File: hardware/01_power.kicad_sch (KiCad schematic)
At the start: 0 parts

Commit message: Power sheet: USB input, rail split, analog LDO
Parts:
- added C1, C2: 1uF, symbol Device:C
- added J1: USB_5V_IN, Connector_RJ:RJ45_Abracon_ARJP11A-MA_Horizontal, symbol Connector_Generic:Conn_01x02
- added R1: 0R, Package_TO_SOT_THT:TO-92_Inline, symbol Device:R
- added U1: MCP1700-3302E/T0, Package_TO_SOT_THT:TO-92_Inline, symbol Regulator_Linear:MCP1700x-330xxTO
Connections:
- new net: C1.1, R1.2, U1.2 (VI)
- new net +3V3_A: C2.1, U1.3 (VO)
- new net +5V: J1.1 (Pin_1), R1.1
- new net GND: C1.2, C2.2, J1.2 (Pin_2), U1.1 (GND)
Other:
- note added: "C1, C2: 1uF per MCP1700 DS20001826F. C2 sets stability; C1 is input decoupling."

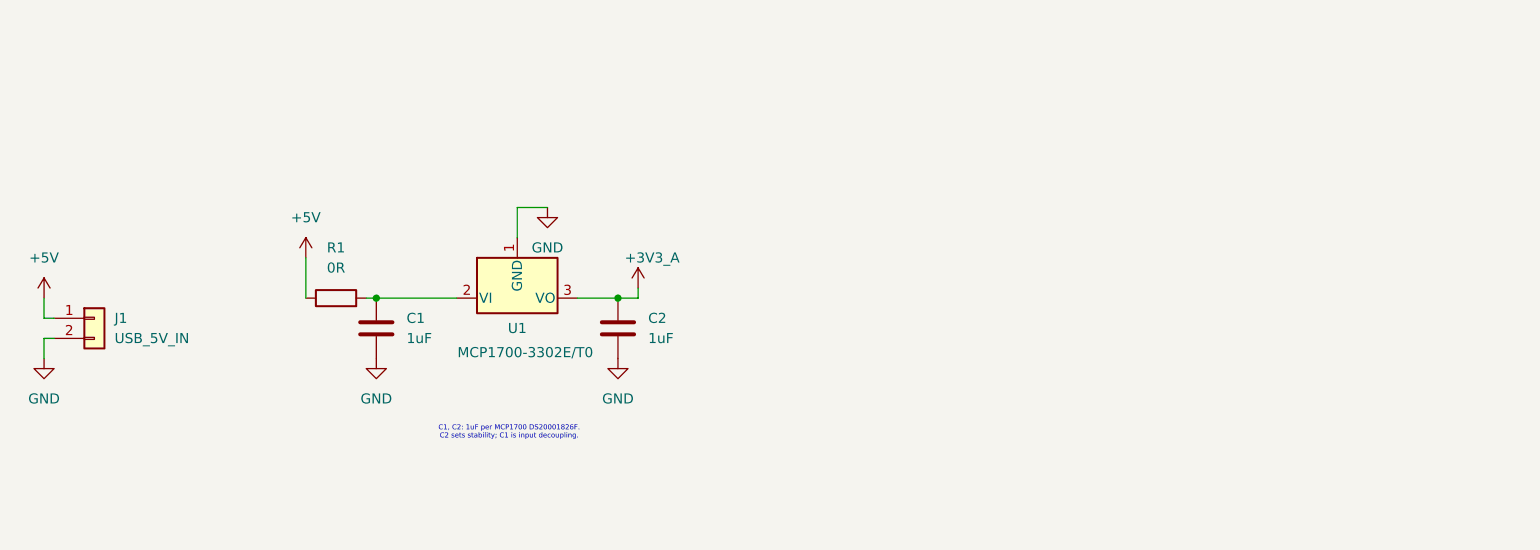
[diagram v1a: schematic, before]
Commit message: Power sheet: analog rail, rail split, 2.2 V reference
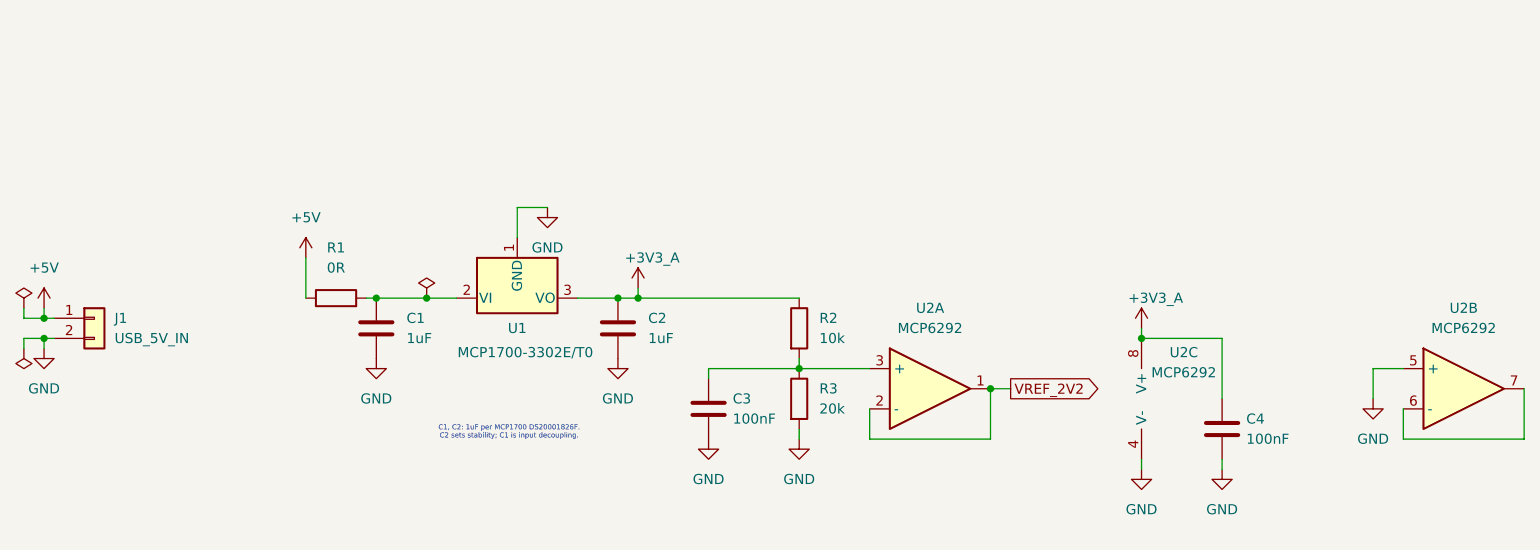
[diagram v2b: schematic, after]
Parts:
- added C3, C4: 100nF, symbol Device:C
- added R2: 10k, symbol Device:R
- added R3: 20k, symbol Device:R
- added U2: MCP6292, Package_TO_SOT_SMD:SOT-353_SC-70-5, symbol Amplifier_Operational:Opamp_Dual
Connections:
- net +3V3_A: now also C4.1, R2.1, U2.8 (V+)
- net GND: now also C3.2, C4.2, R3.2, U2.4 (V-), U2.5 (+)
- new net: U2.6 (-), U2.7
- new net: C3.1, R2.2, R3.1, U2.3 (+)
- new net VREF_2V2: U2.1, U2.2 (-)

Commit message: Add final Rev A schematic PDF and edited footprints
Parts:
- C1, C2, C3, C4: footprint (none) -> Capacitor_THT:C_Disc_D5.0mm_W2.5mm_P5.00mm
- J1: footprint Connector_RJ:RJ45_Abracon_ARJP11A-MA_Horizontal -> Connector_PinHeader_2.54mm:PinHeader_1x02_P2.54mm_Vertical
- R1: footprint Package_TO_SOT_THT:TO-92_Inline -> Resistor_THT:R_Axial_DIN0207_L6.3mm_D2.5mm_P10.16mm_Horizontal
- R2, R3: footprint (none) -> Resistor_THT:R_Axial_DIN0207_L6.3mm_D2.5mm_P10.16mm_Horizontal
- U2: footprint Package_TO_SOT_SMD:SOT-353_SC-70-5 -> Package_DIP:DIP-8_W7.62mm
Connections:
- net +5V_A: now reaches C1.1, R1.2, U1.2 (VI)
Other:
- company: (none) -> Paul Simbulan
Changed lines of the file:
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@@
 	(title_block
 		(title "Oscil")
-		(date "2026-09-18")
-		(rev "0.1")
+		(date "2026-09-21")
+		(rev "A")
+		(company "Paul Simbulan")
 		(comment 1 "Two-channel Digital Oscilloscope and Function Generator")
 		(comment 2 "ESP32-S3 / ESP-IDF / FreeRTOS")
+		(comment 3 "Rev A: breadboard build on ESP32-S3 dev boards")
 	)
 	(text ""
@@
 	)
 	(junction
+		(at 93.98 59.69)
+		(diameter 0)
+		(color 0 0 0 0)
+	)
+	(junction
 		(at 144.78 68.58)
 		(diameter 0)
@@
 	(wire
 		(pts
+			(xy 93.98 59.69) (xy 97.79 59.69)
+		)
+		(stroke
+			(width 0)
+			(type default)
+		)
+	)
+	(wire
+		(pts
 			(xy 144.78 68.58) (xy 153.67 68.58)
 		)
@@
 	(wire
 		(pts
-			(xy 91.44 59.69) (xy 97.79 59.69)
+			(xy 91.44 59.69) (xy 93.98 59.69)
 		)
 		(stroke
@@
 	(wire
 		(pts
+			(xy 93.98 53.34) (xy 93.98 59.69)
+		)
+		(stroke
+			(width 0)
+			(type default)
+		)
+	)
+	(wire
+		(pts
 			(xy 187.96 63.5) (xy 187.96 64.77)
 		)
@@
 			(width 0)
 			(type default)
+		)
+	)
+	(label "+5V_A"
+		(at 93.98 53.34 0)
+		(effects
+			(font
+				(size 1.27 1.27)
+			)
+			(justify left bottom)
 		)
 	)
@@
 			)
 		)
-		(property "Footprint" ""
+		(property "Footprint" "Capacitor_THT:C_Disc_D5.0mm_W2.5mm_P5.00mm"
 			(at 92.4052 67.31 0)
 			(hide yes)
@@
 			)
 		)
-		(property "Footprint" ""
+		(property "Footprint" "Capacitor_THT:C_Disc_D5.0mm_W2.5mm_P5.00mm"
 			(at 122.8852 67.31 0)
 			(hide yes)
@@
 			)
 		)
-		(property "Footprint" "Connector_RJ:RJ45_Abracon_ARJP11A-MA_Horizontal"
+		(property "Footprint" "Connector_PinHeader_2.54mm:PinHeader_1x02_P2.54mm_Vertical"
 			(at 55.88 62.23 0)
 			(hide yes)
@@
 			)
 		)
-		(property "Footprint" "Package_TO_SOT_SMD:SOT-353_SC-70-5"
+		(property "Footprint" "Package_DIP:DIP-8_W7.62mm"
 			(at 228.6 71.12 0)
 			(hide yes)
@@
 			)
 		)
-		(property "Footprint" ""
+		(property "Footprint" "Resistor_THT:R_Axial_DIN0207_L6.3mm_D2.5mm_P10.16mm_Horizontal"
 			(at 143.002 63.5 90)
 			(hide yes)
@@
 			)
 		)
-		(property "Footprint" "Package_TO_SOT_SMD:SOT-353_SC-70-5"
+		(property "Footprint" "Package_DIP:DIP-8_W7.62mm"
 			(at 161.29 71.12 0)
 			(hide yes)
@@
 			)
 		)
-		(property "Footprint" "Package_TO_SOT_THT:TO-92_Inline"
+		(property "Footprint" "Resistor_THT:R_Axial_DIN0207_L6.3mm_D2.5mm_P10.16mm_Horizontal"
 			(at 86.36 61.468 90)
 			(hide yes)
@@
 			)
 		)
-		(property "Footprint" ""
+		(property "Footprint" "Capacitor_THT:C_Disc_D5.0mm_W2.5mm_P5.00mm"
 			(at 199.0852 80.01 0)
 			(hide yes)
@@
 			)
 		)
-		(property "Footprint" ""
+		(property "Footprint" "Capacitor_THT:C_Disc_D5.0mm_W2.5mm_P5.00mm"
 			(at 134.3152 77.47 0)
 			(hide yes)
@@
 			)
 		)
-		(property "Footprint" ""
+		(property "Footprint" "Resistor_THT:R_Axial_DIN0207_L6.3mm_D2.5mm_P10.16mm_Horizontal"
 			(at 143.002 72.39 90)
 			(hide yes)
@@
 			)
 		)
-		(property "Footprint" "Package_TO_SOT_SMD:SOT-353_SC-70-5"
+		(property "Footprint" "Package_DIP:DIP-8_W7.62mm"
 			(at 190.5 72.39 0)
 			(hide yes)

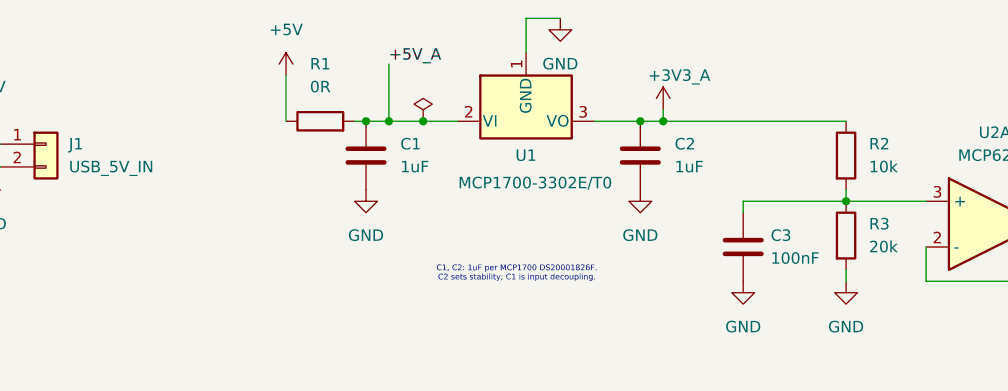
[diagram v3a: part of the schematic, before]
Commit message: hardware: bulk decoupling on the analog rail and ADC VDD, VREF filter, analog parts on +3V3_A
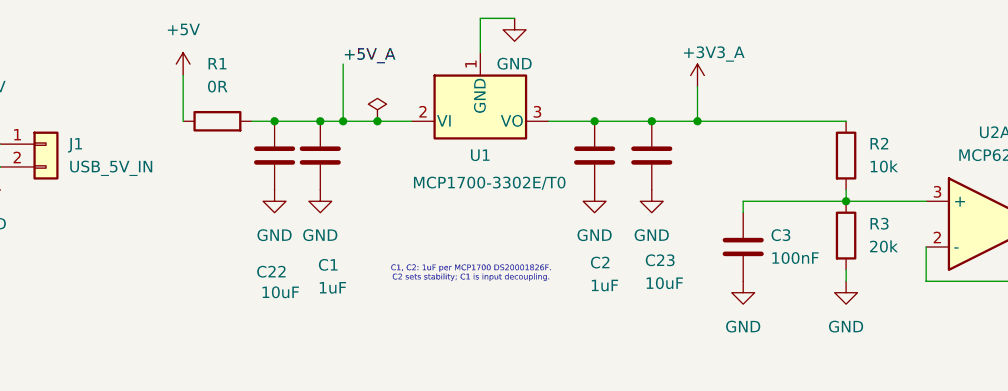
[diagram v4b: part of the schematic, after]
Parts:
- added C22, C23: 10uF, Capacitor_THT:C_Disc_D5.0mm_W2.5mm_P5.00mm, symbol Device:C
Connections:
- net +3V3_A: now also C23.1
- net +5V_A: now also C22.1
- net GND: now also C22.2, C23.2
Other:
- moved on the sheet: C1, C2, R1, U1

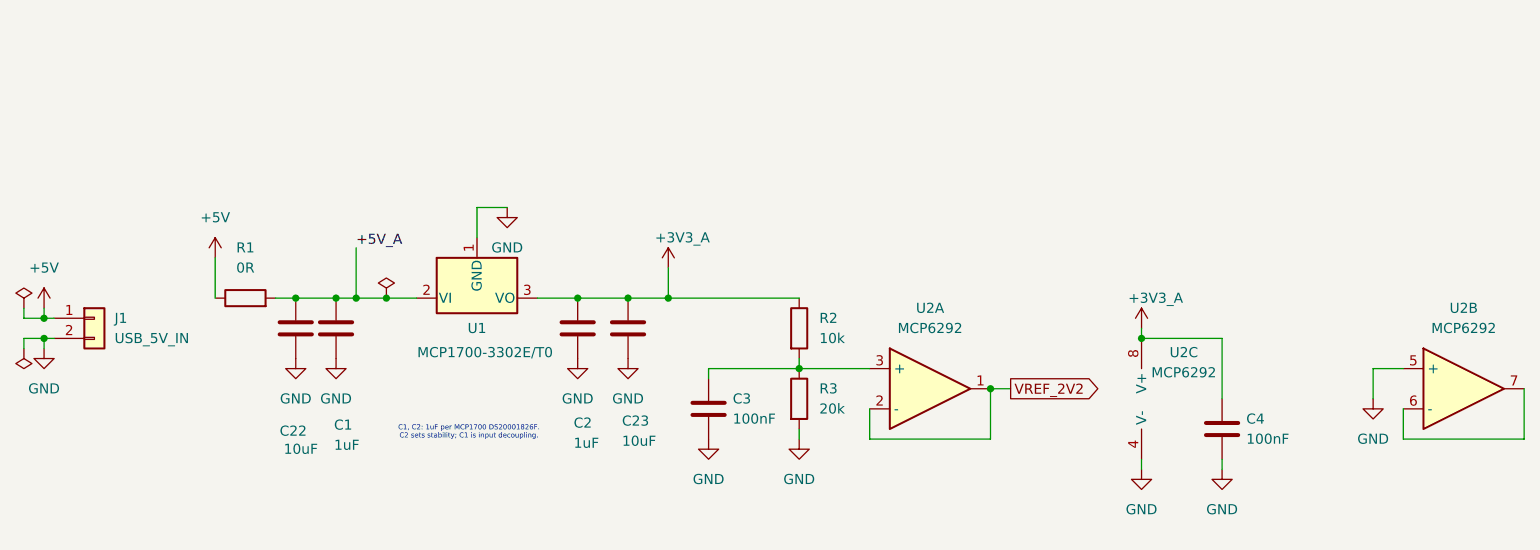
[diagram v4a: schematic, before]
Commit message: hardware: 220R series on each link line, analog decoupling notes
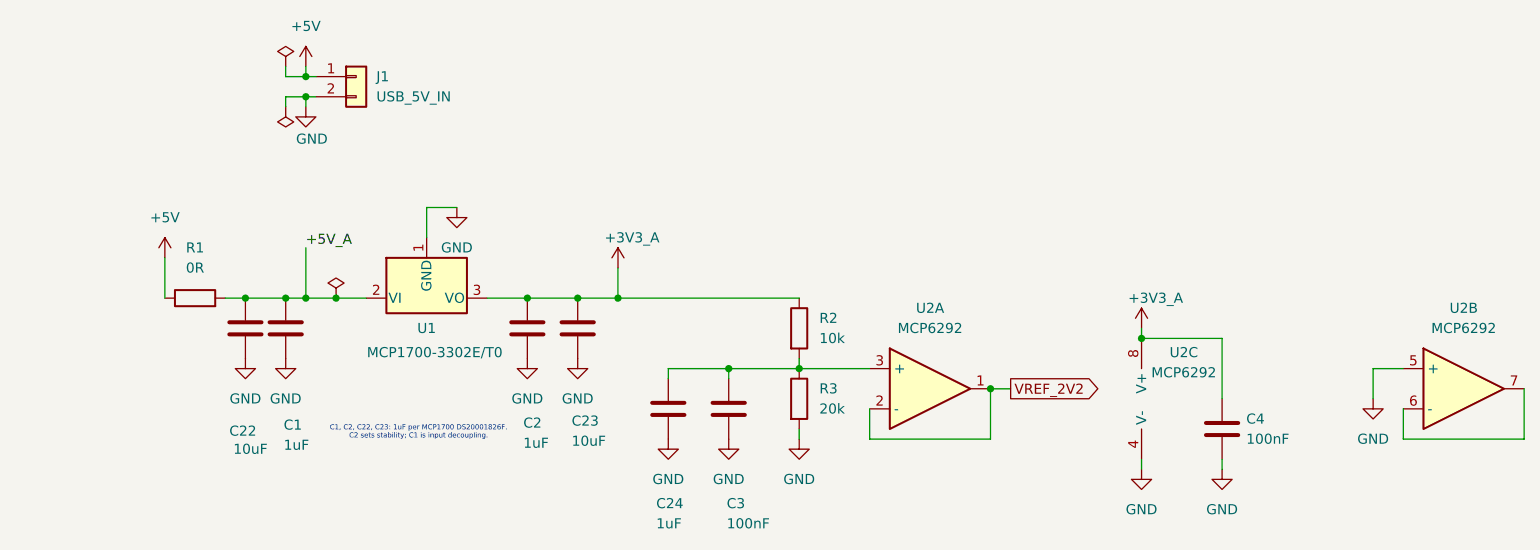
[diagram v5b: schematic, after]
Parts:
- added C24: 1uF, Capacitor_THT:C_Disc_D5.0mm_W2.5mm_P5.00mm, symbol Device:C
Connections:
- net GND: now also C24.2
- net at C3.1, R2.2, R3.1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: now also C24.1
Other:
- note added: "C1, C2, C22, C23: 1uF per MCP1700 DS20001826F. C2 sets stability; C1 is input decoupling."
- note removed: "C1, C2: 1uF per MCP1700 DS20001826F. C2 sets stability; C1 is input decoupling."
- moved on the sheet: C1, C2, C22, C23, C3, J1, R1, U1
